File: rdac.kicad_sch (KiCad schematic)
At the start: 12 parts

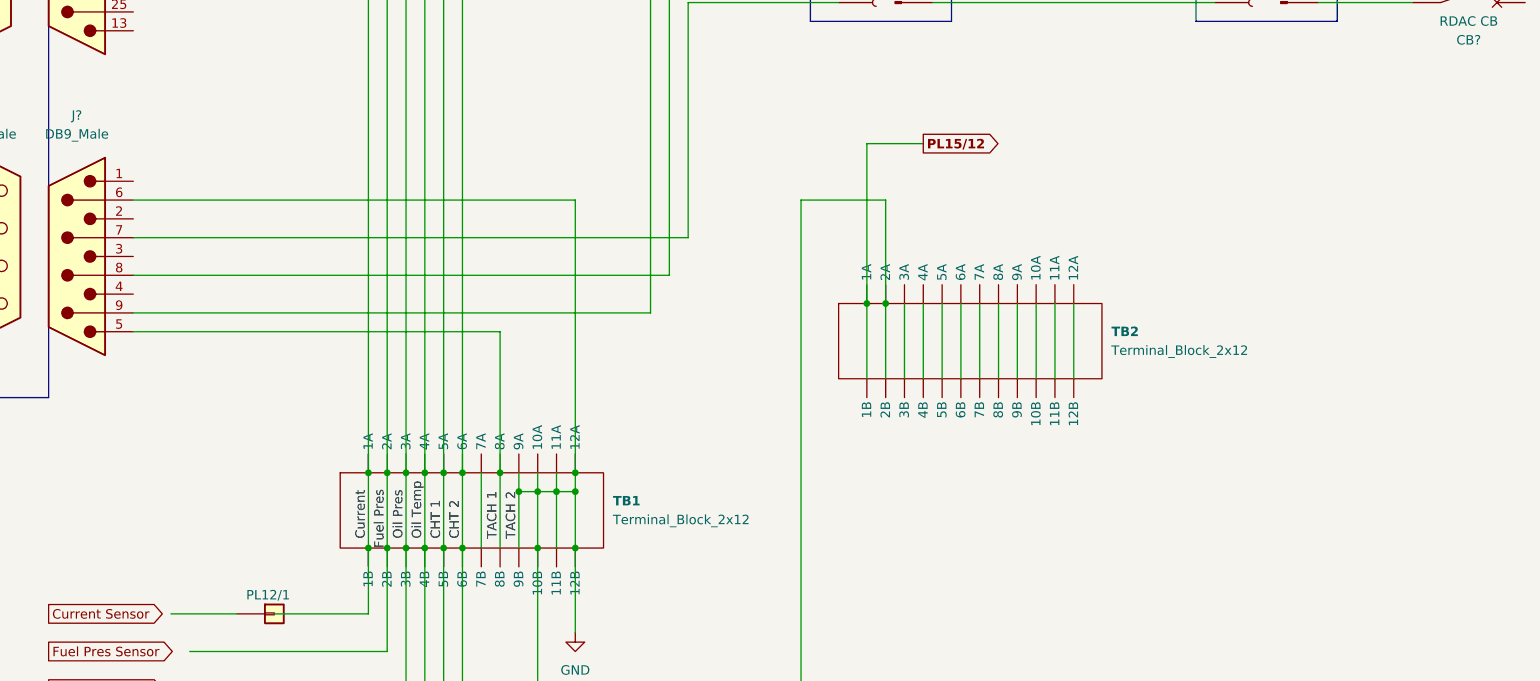
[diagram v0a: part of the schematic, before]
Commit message: Added Main Instrument Panel and Main Bus Panel
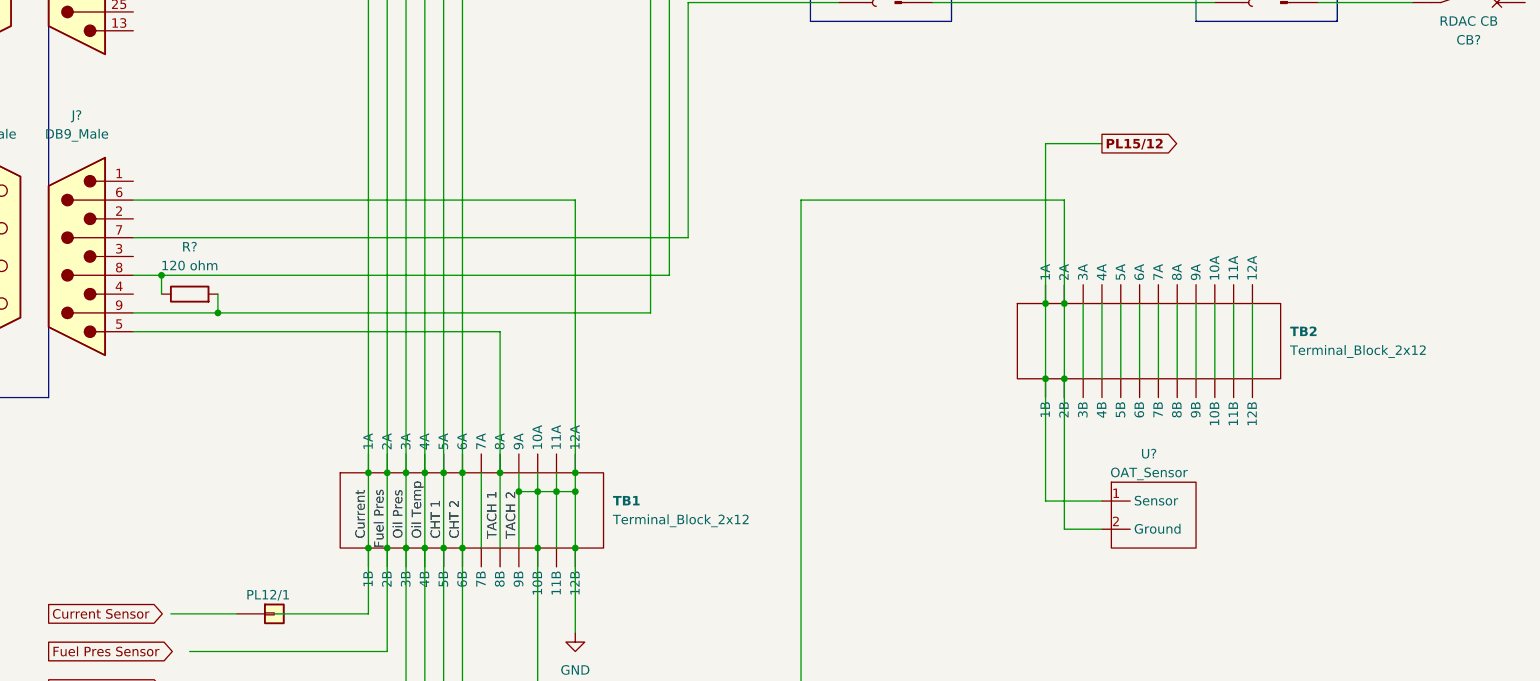
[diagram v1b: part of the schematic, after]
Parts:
- added R?: 120 ohm, symbol Device:R
- added U?: OAT_Sensor, symbol gary aircraft symbol library:OAT_Sensor
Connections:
- net CAN Hi: now also R?.2
- net CAN Lo: now also R?.1
- net GND: now also U?.2 (Ground)
- net PL15/12: now also U?.1 (Sensor)
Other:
- title: (none) -> Europa RDAC wiring
- moved on the sheet: TB2
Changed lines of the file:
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@@
 (kicad_sch (version 20211123) (generator eeschema)
   (paper "A4")
+  (title_block
+    (title "Europa RDAC wiring")
+    (date "2022-12-02")
+    (rev "1")
+  )
   (junction (at 127 147.32) (diameter 0) (color 0 0 0 0)
   )
@@
   (junction (at 114.3 147.32) (diameter 0) (color 0 0 0 0)
   )
+  (junction (at 88.9 125.73) (diameter 0) (color 0 0 0 0)
+  )
   (junction (at 111.76 147.32) (diameter 0) (color 0 0 0 0)
   )
@@
   (junction (at 137.16 147.32) (diameter 0) (color 0 0 0 0)
   )
+  (junction (at 81.28 120.65) (diameter 0) (color 0 0 0 0)
+  )
   (junction (at 114.3 157.48) (diameter 0) (color 0 0 0 0)
   )
   (junction (at 137.16 157.48) (diameter 0) (color 0 0 0 0)
   )
-  (junction (at 179.07 124.46) (diameter 0) (color 0 0 0 0)
-  )
-  (junction (at 176.53 124.46) (diameter 0) (color 0 0 0 0)
+  (junction (at 203.2 124.46) (diameter 0) (color 0 0 0 0)
+  )
+  (junction (at 200.66 124.46) (diameter 0) (color 0 0 0 0)
+  )
+  (junction (at 200.66 134.62) (diameter 0) (color 0 0 0 0)
   )
   (junction (at 116.84 157.48) (diameter 0) (color 0 0 0 0)
@@
   (junction (at 111.76 157.48) (diameter 0) (color 0 0 0 0)
   )
+  (junction (at 203.2 134.62) (diameter 0) (color 0 0 0 0)
+  )
   (wire (pts (xy 82.55 191.77) (xy 121.92 191.77))
     (stroke (width 0) (type default) (color 0 0 0 0))
@@
     (stroke (width 0) (type dot) (color 0 0 0 0))
   )
-  (wire (pts (xy 77.47 125.73) (xy 147.32 125.73))
-    (stroke (width 0) (type default) (color 0 0 0 0))
-  )
-  (wire (pts (xy 179.07 124.46) (xy 179.07 134.62))
-    (stroke (width 0) (type dot) (color 0 0 0 0))
-  )
-  (wire (pts (xy 189.23 124.46) (xy 189.23 134.62))
-    (stroke (width 0) (type dot) (color 0 0 0 0))
+  (wire (pts (xy 77.47 125.73) (xy 88.9 125.73))
+    (stroke (width 0) (type default) (color 0 0 0 0))
+  )
+  (wire (pts (xy 203.2 124.46) (xy 203.2 134.62))
+    (stroke (width 0) (type dot) (color 0 0 0 0))
+  )
+  (wire (pts (xy 213.36 124.46) (xy 213.36 134.62))
+    (stroke (width 0) (type dot) (color 0 0 0 0))
+  )
+  (wire (pts (xy 203.2 154.94) (xy 208.28 154.94))
+    (stroke (width 0) (type default) (color 0 0 0 0))
   )
   (wire (pts (xy 147.32 78.74) (xy 172.72 78.74))
     (stroke (width 0) (type default) (color 0 0 0 0))
   )
+  (wire (pts (xy 81.28 120.65) (xy 149.86 120.65))
+    (stroke (width 0) (type default) (color 0 0 0 0))
+  )
   (wire (pts (xy 119.38 147.32) (xy 119.38 157.48))
     (stroke (width 0) (type dot) (color 0 0 0 0))
@@
     (stroke (width 0) (type default) (color 0 0 0 0))
   )
-  (wire (pts (xy 201.93 124.46) (xy 201.93 134.62))
-    (stroke (width 0) (type dot) (color 0 0 0 0))
-  )
-  (wire (pts (xy 167.64 110.49) (xy 179.07 110.49))
+  (wire (pts (xy 226.06 124.46) (xy 226.06 134.62))
+    (stroke (width 0) (type dot) (color 0 0 0 0))
+  )
+  (wire (pts (xy 167.64 110.49) (xy 203.2 110.49))
     (stroke (width 0) (type default) (color 0 0 0 0))
   )
@@
     (stroke (width 0) (type default) (color 0 0 0 0))
   )
-  (wire (pts (xy 186.69 124.46) (xy 186.69 134.62))
-    (stroke (width 0) (type dot) (color 0 0 0 0))
-  )
-  (wire (pts (xy 176.53 124.46) (xy 176.53 134.62))
-    (stroke (width 0) (type dot) (color 0 0 0 0))
-  )
-  (wire (pts (xy 194.31 124.46) (xy 194.31 134.62))
+  (wire (pts (xy 210.82 124.46) (xy 210.82 134.62))
+    (stroke (width 0) (type dot) (color 0 0 0 0))
+  )
+  (wire (pts (xy 200.66 124.46) (xy 200.66 134.62))
+    (stroke (width 0) (type dot) (color 0 0 0 0))
+  )
+  (wire (pts (xy 218.44 124.46) (xy 218.44 134.62))
     (stroke (width 0) (type dot) (color 0 0 0 0))
   )
@@
     (stroke (width 0) (type default) (color 0 0 0 0))
   )
-  (wire (pts (xy 199.39 124.46) (xy 199.39 134.62))
+  (wire (pts (xy 200.66 134.62) (xy 200.66 151.13))
+    (stroke (width 0) (type default) (color 0 0 0 0))
+  )
+  (wire (pts (xy 223.52 124.46) (xy 223.52 134.62))
     (stroke (width 0) (type dot) (color 0 0 0 0))
   )
@@
     (stroke (width 0) (type default) (color 0 0 0 0))
   )
-  (wire (pts (xy 77.47 120.65) (xy 149.86 120.65))
+  (wire (pts (xy 77.47 120.65) (xy 81.28 120.65))
     (stroke (width 0) (type default) (color 0 0 0 0))
   )
@@
     (stroke (width 0) (type default) (color 0 0 0 0))
   )
-  (wire (pts (xy 176.53 102.87) (xy 184.15 102.87))
-    (stroke (width 0) (type default) (color 0 0 0 0))
-  )
-  (wire (pts (xy 191.77 124.46) (xy 191.77 134.62))
+  (wire (pts (xy 200.66 102.87) (xy 208.28 102.87))
+    (stroke (width 0) (type default) (color 0 0 0 0))
+  )
+  (wire (pts (xy 215.9 124.46) (xy 215.9 134.62))
     (stroke (width 0) (type dot) (color 0 0 0 0))
   )
@@
     (stroke (width 0) (type default) (color 0 0 0 0))
   )
-  (wire (pts (xy 181.61 124.46) (xy 181.61 134.62))
+  (wire (pts (xy 205.74 124.46) (xy 205.74 134.62))
     (stroke (width 0) (type dot) (color 0 0 0 0))
   )
@@
     (stroke (width 0) (type default) (color 0 0 0 0))
   )
+  (wire (pts (xy 81.28 120.65) (xy 81.28 123.19))
+    (stroke (width 0) (type default) (color 0 0 0 0))
+  )
   (wire (pts (xy 77.47 59.69) (xy 119.38 59.69))
     (stroke (width 0) (type default) (color 0 0 0 0))
@@
     (stroke (width 0) (type default) (color 0 0 0 0))
   )
+  (wire (pts (xy 203.2 134.62) (xy 203.2 154.94))
+    (stroke (width 0) (type default) (color 0 0 0 0))
+  )
   (wire (pts (xy 77.47 110.49) (xy 137.16 110.49))
     (stroke (width 0) (type default) (color 0 0 0 0))
@@
     (stroke (width 0) (type dot) (color 0 0 0 0))
   )
+  (wire (pts (xy 200.66 151.13) (xy 208.28 151.13))
+    (stroke (width 0) (type default) (color 0 0 0 0))
+  )
   (wire (pts (xy 185.42 81.28) (xy 223.52 81.28))
     (stroke (width 0) (type default) (color 0 0 0 0))
   )
-  (wire (pts (xy 176.53 124.46) (xy 176.53 102.87))
+  (wire (pts (xy 200.66 124.46) (xy 200.66 102.87))
     (stroke (width 0) (type default) (color 0 0 0 0))
   )
@@
     (stroke (width 0) (type default) (color 0 0 0 0))
   )
-  (wire (pts (xy 179.07 110.49) (xy 179.07 124.46))
+  (wire (pts (xy 203.2 110.49) (xy 203.2 124.46))
     (stroke (width 0) (type default) (color 0 0 0 0))
   )
@@
     (stroke (width 0) (type default) (color 0 0 0 0))
   )
-  (wire (pts (xy 184.15 124.46) (xy 184.15 134.62))
-    (stroke (width 0) (type dot) (color 0 0 0 0))
-  )
-  (wire (pts (xy 204.47 124.46) (xy 204.47 134.62))
+  (wire (pts (xy 208.28 124.46) (xy 208.28 134.62))
+    (stroke (width 0) (type dot) (color 0 0 0 0))
+  )
+  (wire (pts (xy 88.9 123.19) (xy 88.9 125.73))
+    (stroke (width 0) (type default) (color 0 0 0 0))
+  )
+  (wire (pts (xy 228.6 124.46) (xy 228.6 134.62))
     (stroke (width 0) (type dot) (color 0 0 0 0))
   )
@@
     (stroke (width 0) (type default) (color 0 0 0 0))
   )
+  (wire (pts (xy 88.9 125.73) (xy 147.32 125.73))
+    (stroke (width 0) (type default) (color 0 0 0 0))
+  )
   (wire (pts (xy 77.47 115.57) (xy 152.4 115.57))
     (stroke (width 0) (type default) (color 0 0 0 0))
@@
     (stroke (width 0) (type default) (color 0 0 0 0))
   )
-  (wire (pts (xy 196.85 124.46) (xy 196.85 134.62))
+  (wire (pts (xy 220.98 124.46) (xy 220.98 134.62))
     (stroke (width 0) (type dot) (color 0 0 0 0))
   )
@@
     )
   )
-  (global_label "PL15{slash}12" (shape output) (at 184.15 102.87 0) (fields_autoplaced)
+  (global_label "PL15{slash}12" (shape output) (at 208.28 102.87 0) (fields_autoplaced)
     (effects (font (size 1.27 1.27) bold) (justify left))
-    (property "Intersheet References" "${INTERSHEET_REFS}" (id 0) (at 195.2202 102.743 0)
+    (property "Intersheet References" "${INTERSHEET_REFS}" (id 0) (at 219.3502 102.743 0)
       (effects (font (size 1.27 1.27) bold) (justify left) hide)
     )
@@
     )
     (pin "1")
+  )
+  (symbol (lib_id "gary aircraft symbol library:OAT_Sensor") (at 214.63 146.05 0) (unit 1)
+    (in_bom yes) (on_board no)
+    (property "Reference" "U?" (id 0) (at 214.63 144.78 0))
+    (property "Value" "OAT_Sensor" (id 1) (at 214.63 147.32 0))
+    (property "Footprint" "" (id 2) (at 214.63 146.05 0)
+      (effects (font (size 1.27 1.27)) hide)
+    )
+    (property "Datasheet" "" (id 3) (at 214.63 146.05 0)
+      (effects (font (size 1.27 1.27)) hide)
+    )
+    (pin "1")
+    (pin "2")
   )
   (symbol (lib_name "Conn_01x03_Female_1") (lib_id "Connector:Conn_01x03_Female") (at 228.6 81.28 0) (unit 1)
@@
     (pin "9")
   )
-  (symbol (lib_id "gary aircraft symbol library:Terminal_Block_2x12") (at 189.23 111.76 0) (unit 1)
+  (symbol (lib_id "gary aircraft symbol library:Terminal_Block_2x12") (at 213.36 111.76 0) (unit 1)
     (in_bom yes) (on_board yes) (fields_autoplaced)
-    (property "Reference" "TB2" (id 0) (at 209.55 128.2699 0)
+    (property "Reference" "TB2" (id 0) (at 233.68 128.2699 0)
       (effects (font (size 1.27 1.27) bold) (justify left))
     )
-    (property "Value" "Terminal_Block_2x12" (id 1) (at 209.55 130.8099 0)
+    (property "Value" "Terminal_Block_2x12" (id 1) (at 233.68 130.8099 0)
       (effects (font (size 1.27 1.27)) (justify left))
     )
-    (property "Footprint" "" (id 2) (at 189.23 111.76 0)
-      (effects (font (size 1.27 1.27)) hide)
-    )
-    (property "Datasheet" "" (id 3) (at 189.23 111.76 0)
+    (property "Footprint" "" (id 2) (at 213.36 111.76 0)
+      (effects (font (size 1.27 1.27)) hide)
+    )
+    (property "Datasheet" "" (id 3) (at 213.36 111.76 0)
       (effects (font (size 1.27 1.27)) hide)
     )
@@
     (pin "9")
   )
+  (symbol (lib_id "Device:R") (at 85.09 123.19 90) (unit 1)
+    (in_bom yes) (on_board yes) (fields_autoplaced)
+    (property "Reference" "R?" (id 0) (at 85.09 116.84 90))
+    (property "Value" "120 ohm" (id 1) (at 85.09 119.38 90))
+    (property "Footprint" "" (id 2) (at 85.09 124.968 90)
+      (effects (font (size 1.27 1.27)) hide)
+    )
+    (property "Datasheet" "~" (id 3) (at 85.09 123.19 0)
+      (effects (font (size 1.27 1.27)) hide)
+    )
+    (pin "1")
+    (pin "2")
+  )
 )

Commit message: Proof reading and snagging updates
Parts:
- added FB2/1, FB2/4: Fuse, symbol Device:Fuse
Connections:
- net +12 volt: no longer J?.7, PL10-F.3 (Pin_3)
- net 15: now also FB2/1.2; no longer PL10-M.3 (Pin_3)
- net +12v TB5/1: now reaches CB?.1
- new net: FB2/4.1, J?.7
- new net: FB2/1.1, FB2/4.2
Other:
- moved on the sheet: CB?, PL10-F, PL10-M, PL15

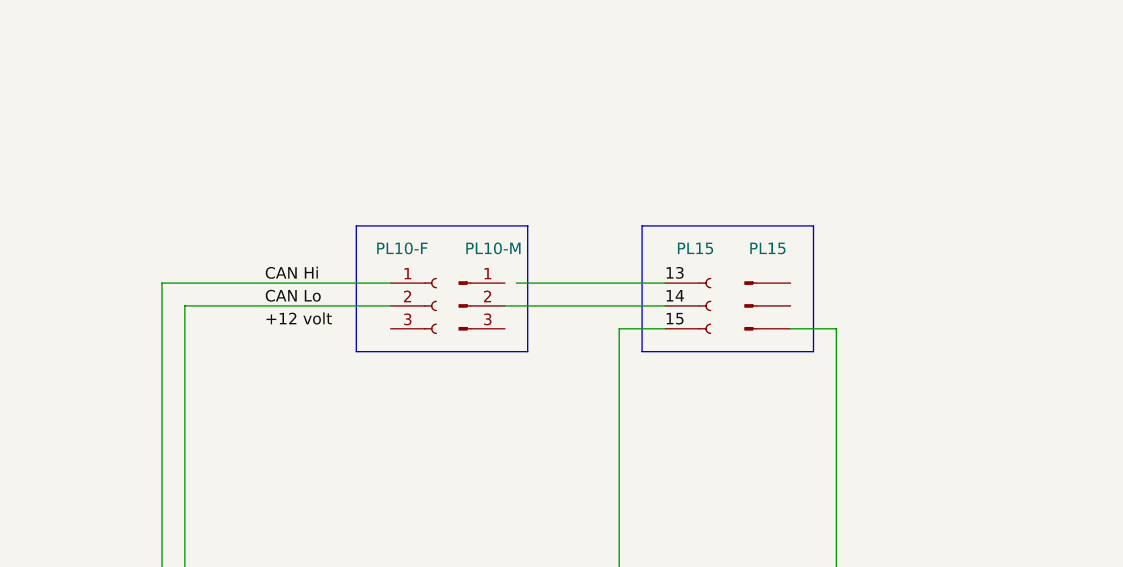
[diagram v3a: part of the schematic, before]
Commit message: Updates from manual validation
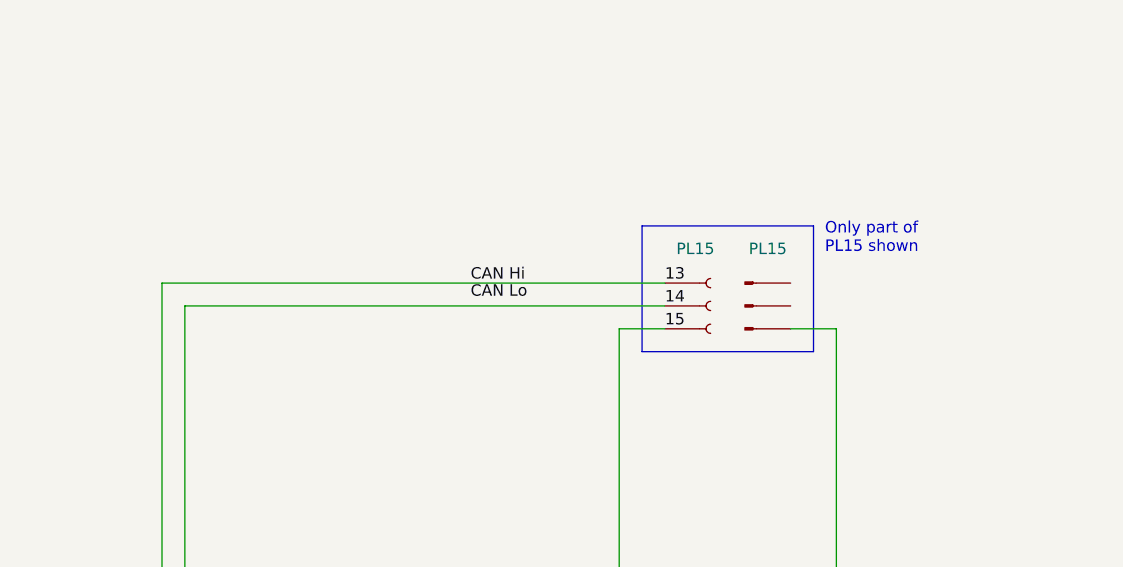
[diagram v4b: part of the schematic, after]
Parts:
- removed PL10-F: Conn_01x03_Female, symbol Connector:Conn_01x03_Female
- removed PL10-M: Conn_01x03_Male, symbol Connector:Conn_01x03_Male
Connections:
- net CAN Hi is gone; now on net 13: J?.9, R?.2
- net 14: now also J?.8, R?.1
- net CAN Lo: no longer J?.8, R?.1
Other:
- note added: "Only part of PL15 shown"
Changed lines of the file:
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@@
   (title_block
     (title "Europa RDAC wiring")
-    (date "2022-12-22")
-    (rev "1")
+    (date "2022-12-24")
+    (rev "2")
   )
   (junction (at 127 147.32) (diameter 0) (color 0 0 0 0)
@@
     (stroke (width 0) (type default) (color 0 0 0 0))
   )
-  (wire (pts (xy 147.32 48.26) (xy 172.72 48.26))
-    (stroke (width 0) (type default) (color 0 0 0 0))
-  )
   (wire (pts (xy 81.28 120.65) (xy 149.86 120.65))
     (stroke (width 0) (type default) (color 0 0 0 0))
@@
     (stroke (width 0) (type dot) (color 0 0 0 0))
   )
-  (wire (pts (xy 186.69 48.26) (xy 203.2 48.26))
+  (wire (pts (xy 147.32 48.26) (xy 203.2 48.26))
     (stroke (width 0) (type default) (color 0 0 0 0))
   )
@@
     (stroke (width 0) (type default) (color 0 0 0 0))
   )
-  (wire (pts (xy 149.86 50.8) (xy 172.72 50.8))
+  (wire (pts (xy 149.86 50.8) (xy 203.2 50.8))
     (stroke (width 0) (type default) (color 0 0 0 0))
   )
@@
     (stroke (width 0) (type default) (color 0 0 0 0))
   )
-  (polyline (pts (xy 187.96 41.91) (xy 187.96 55.88))
-    (stroke (width 0) (type default) (color 0 0 0 0))
-  )
   (wire (pts (xy 149.86 120.65) (xy 149.86 50.8))
     (stroke (width 0) (type default) (color 0 0 0 0))
@@
     (stroke (width 0) (type default) (color 0 0 0 0))
   )
-  (polyline (pts (xy 168.91 41.91) (xy 187.96 41.91))
-    (stroke (width 0) (type default) (color 0 0 0 0))
-  )
-  (polyline (pts (xy 168.91 41.91) (xy 168.91 55.88))
-    (stroke (width 0) (type default) (color 0 0 0 0))
-  )
   (wire (pts (xy 81.28 120.65) (xy 81.28 123.19))
     (stroke (width 0) (type default) (color 0 0 0 0))
@@
     (stroke (width 0) (type default) (color 0 0 0 0))
   )
-  (wire (pts (xy 185.42 50.8) (xy 203.2 50.8))
-    (stroke (width 0) (type default) (color 0 0 0 0))
-  )
   (wire (pts (xy 200.66 124.46) (xy 200.66 102.87))
     (stroke (width 0) (type default) (color 0 0 0 0))
@@
   )
   (wire (pts (xy 222.25 86.36) (xy 222.25 53.34))
-    (stroke (width 0) (type default) (color 0 0 0 0))
-  )
-  (polyline (pts (xy 187.96 55.88) (xy 168.91 55.88))
     (stroke (width 0) (type default) (color 0 0 0 0))
   )
@@
     (effects (font (size 1.27 1.27) (thickness 0.254) bold) (justify left bottom))
   )
+  (text "Only part of\nPL15 shown" (at 220.98 45.085 0)
+    (effects (font (size 1.27 1.27)) (justify left bottom))
+  )
   (label "14" (at 203.2 50.8 0)
     (effects (font (size 1.27 1.27)) (justify left bottom))
@@
     (effects (font (size 1.27 1.27)) (justify left bottom))
   )
-  (label "CAN Lo" (at 158.75 50.8 0)
-    (effects (font (size 1.27 1.27)) (justify left bottom))
-  )
-  (label "CAN Hi" (at 158.75 48.26 0)
+  (label "CAN Lo" (at 181.61 50.165 0)
     (effects (font (size 1.27 1.27)) (justify left bottom))
   )
@@
     (effects (font (size 1.27 1.27)) (justify left bottom))
   )
-  (label "+12 volt" (at 158.75 53.34 0)
-    (effects (font (size 1.27 1.27)) (justify left bottom))
-  )
   (label "TACH 2" (at 129.54 156.21 90)
     (effects (font (size 1.27 1.27)) (justify left bottom))
@@
   )
   (label "Oil Temp" (at 116.84 156.21 90)
+    (effects (font (size 1.27 1.27)) (justify left bottom))
+  )
+  (label "CAN Hi" (at 181.61 48.26 0)
     (effects (font (size 1.27 1.27)) (justify left bottom))
   )
@@
     (pin "")
   )
-  (symbol (lib_id "Connector:Conn_01x03_Male") (at 180.34 50.8 0) (unit 1)
-    (in_bom yes) (on_board yes)
-    (property "Reference" "PL10-M" (id 0) (at 184.15 44.45 0))
-    (property "Value" "Conn_01x03_Male" (id 1) (at 186.69 59.69 0)
-      (effects (font (size 1.27 1.27)) hide)
-    )
-    (property "Footprint" "" (id 2) (at 180.34 50.8 0)
-      (effects (font (size 1.27 1.27)) hide)
-    )
-    (property "Datasheet" "~" (id 3) (at 180.34 50.8 0)
-      (effects (font (size 1.27 1.27)) hide)
-    )
-    (pin "1")
-    (pin "2")
-    (pin "3")
-  )
   (symbol (lib_id "Connector:DB25_Male") (at 69.85 57.15 180) (unit 1)
     (in_bom yes) (on_board yes) (fields_autoplaced)
@@
     (pin "9")
   )
-  (symbol (lib_id "Connector:Conn_01x03_Female") (at 177.8 50.8 0) (unit 1)
-    (in_bom yes) (on_board yes)
-    (property "Reference" "PL10-F" (id 0) (at 173.99 44.45 0))
-    (property "Value" "Conn_01x03_Female" (id 1) (at 166.37 43.18 0)
-      (effects (font (size 1.27 1.27)) hide)
-    )
-    (property "Footprint" "" (id 2) (at 177.8 50.8 0)
-      (effects (font (size 1.27 1.27)) hide)
-    )
-    (property "Datasheet" "~" (id 3) (at 177.8 50.8 0)
-      (effects (font (size 1.27 1.27)) hide)
-    )
-    (pin "1")
-    (pin "2")
-    (pin "3")
-  )
   (symbol (lib_id "Connector:DB9_Male") (at 69.85 118.11 180) (unit 1)
